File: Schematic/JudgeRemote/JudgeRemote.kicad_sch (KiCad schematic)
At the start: 34 parts, among them J1 Battery IN, J10 Solenoid, J6 I2C Out, SW2 Button A, SW2 Button B, SW2 Button C, SW2 Button D, SW2 Button E, SW2 Button F, SW2 Button G, SW2 Button H, U1 ESP32-DevKitC, U2 Mini360

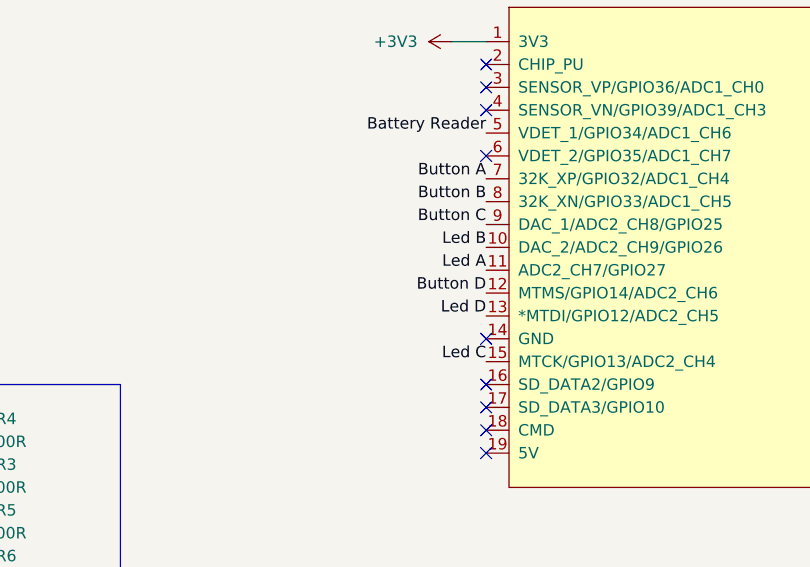
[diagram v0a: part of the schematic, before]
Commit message: add led support to remote and box
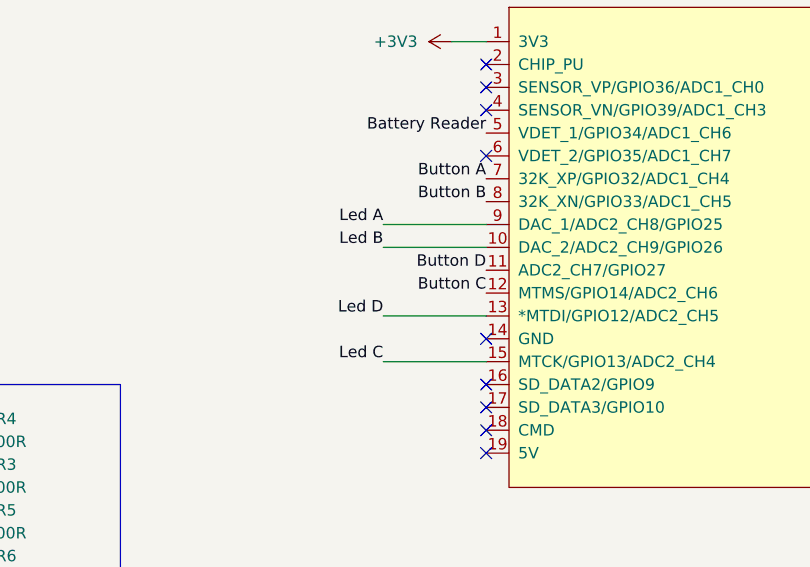
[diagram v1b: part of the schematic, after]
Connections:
- net Button C: now also U1.12 (MTMS/GPIO14/ADC2_CH6); no longer U1.9 (DAC_1/ADC2_CH8/GPIO25)
- net Button D: now also U1.11 (ADC2_CH7/GPIO27); no longer U1.12 (MTMS/GPIO14/ADC2_CH6)
- net Led A: now also U1.9 (DAC_1/ADC2_CH8/GPIO25); no longer U1.11 (ADC2_CH7/GPIO27)
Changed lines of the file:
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@@
+    (stroke (width 0) (type default))
+  )
+  (wire (pts (xy 128.27 64.77) (xy 139.7 64.77))
     (stroke (width 0) (type default))
   )
@@
     (stroke (width 0) (type default))
   )
+  (wire (pts (xy 128.27 54.61) (xy 139.7 54.61))
+    (stroke (width 0) (type default))
+  )
   (wire (pts (xy 30.48 30.48) (xy 35.56 30.48))
     (stroke (width 0) (type default))
   )
   (wire (pts (xy 73.66 87.63) (xy 73.66 92.71))
+    (stroke (width 0) (type default))
+  )
+  (wire (pts (xy 128.27 57.15) (xy 139.7 57.15))
+    (stroke (width 0) (type default))
+  )
+  (wire (pts (xy 128.27 69.85) (xy 139.7 69.85))
     (stroke (width 0) (type default))
   )
@@
     (effects (font (size 1.27 1.27)) (justify left bottom))
   )
-  (label "Button D" (at 139.7 62.23 180) (fields_autoplaced)
+  (label "Button D" (at 139.7 59.69 180) (fields_autoplaced)
     (effects (font (size 1.27 1.27)) (justify right bottom))
   )
@@
     (effects (font (size 1.27 1.27)) (justify left bottom))
   )
-  (label "Led B" (at 139.7 57.15 180) (fields_autoplaced)
+  (label "Led B" (at 128.27 57.15 180) (fields_autoplaced)
     (effects (font (size 1.27 1.27)) (justify right bottom))
   )
@@
     (effects (font (size 1.27 1.27)) (justify right bottom))
   )
-  (label "Led D" (at 139.7 64.77 180) (fields_autoplaced)
+  (label "Led D" (at 128.27 64.77 180) (fields_autoplaced)
     (effects (font (size 1.27 1.27)) (justify right bottom))
   )
@@
     (effects (font (size 1.27 1.27)) (justify right bottom))
   )
-  (label "Led C" (at 139.7 69.85 180) (fields_autoplaced)
+  (label "Led C" (at 128.27 69.85 180) (fields_autoplaced)
     (effects (font (size 1.27 1.27)) (justify right bottom))
   )
@@
     (effects (font (size 1.27 1.27)) (justify left bottom))
   )
-  (label "Led A" (at 139.7 59.69 180) (fields_autoplaced)
+  (label "Led A" (at 128.27 54.61 180) (fields_autoplaced)
     (effects (font (size 1.27 1.27)) (justify right bottom))
   )
@@
     (effects (font (size 1.27 1.27)) (justify right bottom))
   )
-  (label "Button C" (at 139.7 54.61 180) (fields_autoplaced)
-    (effects (font (size 1.27 1.27)) (justify right bottom))
-  )
+  (label "Button C" (at 139.7 62.23 180) (fields_autoplaced)
+    (effects (font (size 1.27 1.27)) (justify right bottom))
+  )
